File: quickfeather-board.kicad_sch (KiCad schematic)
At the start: 101 parts, among them IC1 EOSAI-S-PUN64, J1 PinHeader_1x2_P2.54mm_Drill1.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, J2 PinHeader_1x12_P2.54m_Drill1.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, J3 61301611121, J4 S2B-PH-SM4-TB(LF)(SN), J5 USB-Micro-B_Molex_473460001, J6 PinHeader_2x5_P1.27mm_SMD_Lat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, J7 PinHeader_1x2_P2.54mm_Drill1.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, J8 PinHeader_2x8_P2.54mm_Drill1mm, Q1 NX3008CBKV, Q2 2N7002PV, Q3 2N7002PV, Q4 DMG1012T-7, U1 TPS62821DLCR, U2 MCP73831T-2AC_SOT, U3 GD25Q16CWIGR, U4 DPS310, U5 MC3635, X1 Resonator_32.768kHz_ECX-31B

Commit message: [#54927] Update components
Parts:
- J2: footprint quickfeather-board-footprints:PinHeader_1x12_P2.54_Drill1.1mm -> quickfeather-board-footprints:PinHeader_1x12_P2.54mm_Drill1.1mm
- J3: footprint quickfeather-board-footprints:PinHeader_1x16_P2.54_Drill1.1mm -> quickfeather-board-footprints:PinHeader_1x16_P2.54mm_Drill1.1mm
- J8: footprint quickfeather-board-footprints:PinHeadder_2x8_P2.54mm_Drill1.1mm -> quickfeather-board-footprints:PinHeader_2x8_P2.54mm_Drill1.1mm
- L1: Val (none) -> 470n/3.6A
- U1: footprint quickfeather-board-footprints:QFN-8_2x1mm -> quickfeather-board-footprints:QFN-8_2x1.5mm
- U4: footprint quickfeather-board-footprints:PG-VLGA-8-2 -> quickfeather-board-footprints:LGA-8_2x2.5mm
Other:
- moved on the sheet: C1, C10, C11, C12, C13, C14, C15, C16, C17, C18, C19, C2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

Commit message: [#54927] Update QFN blend file
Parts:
- IC1: footprint quickfeather-board-footprints:QFN-64-1EP_8.5x8.5mm_P0.5mm_EP3.3x3.3mm -> quickfeather-board-footprints:QFN-64-1EP_8.5x8.5mm_P0.5mm_Layout17x15_EP3.3x3.3mm
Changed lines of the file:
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@@
       (effects (font (size 1.27 1.27)) (justify left bottom) hide)
     )
-    (property "Footprint" "quickfeather-board-footprints:QFN-64-1EP_8.5x8.5mm_P0.5mm_EP3.3x3.3mm" (at 172.72 34.29 0)
+    (property "Footprint" "quickfeather-board-footprints:QFN-64-1EP_8.5x8.5mm_P0.5mm_Layout17x15_EP3.3x3.3mm" (at 172.72 34.29 0)
       (effects (font (size 1.27 1.27)) (justify left bottom) hide)
     )

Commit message: [#54927] Fix DNP
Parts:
- J2, J3, J8, R21, R22, R36: now not fitted; now left out of the parts list
- R42: DNP 1 -> DNP; now not fitted; now left out of the parts list
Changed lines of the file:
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@@
   )
   (symbol (lib_id "quickfeather-board:R_10k_0402") (at 193.675 177.8 270) (unit 1)
-    (in_bom yes) (on_board yes) (dnp no)
+    (in_bom no) (on_board yes) (dnp yes)
     (property "Reference" "R21" (at 194.945 179.07 90)
       (effects (font (size 1.524 1.524)) (justify left))
@@
     )
     (property "DNP" "DNP" (at 193.675 180.34 0)
-      (effects (font (size 1.27 1.27)))
+      (effects (font (size 1.27 1.27)) hide)
     )
     (property "License" "Apache-2.0" (at 168.275 198.12 0)
@@
   )
   (symbol (lib_id "quickfeather-board:R_10k_0402") (at 179.705 182.88 90) (unit 1)
-    (in_bom yes) (on_board yes) (dnp no)
+    (in_bom no) (on_board yes) (dnp yes)
     (property "Reference" "R22" (at 180.975 179.07 90)
       (effects (font (size 1.524 1.524)) (justify right))
@@
     )
     (property "DNP" "DNP" (at 179.705 180.34 0)
-      (effects (font (size 1.27 1.27)))
+      (effects (font (size 1.27 1.27)) hide)
     )
     (property "License" "Apache-2.0" (at 205.105 162.56 0)
@@
   )
   (symbol (lib_id "quickfeather-board:R_10k_0402") (at 255.905 178.435 270) (unit 1)
-    (in_bom yes) (on_board yes) (dnp no)
+    (in_bom no) (on_board yes) (dnp yes)
     (property "Reference" "R36" (at 257.175 179.705 90)
       (effects (font (size 1.524 1.524)) (justify left))
@@
     )
     (property "DNP" "DNP" (at 255.905 179.07 0)
-      (effects (font (size 1.27 1.27)) (justify left))
+      (effects (font (size 1.27 1.27)) (justify left) hide)
     )
     (property "License" "Apache-2.0" (at 230.505 198.755 0)
@@
   )
   (symbol (lib_id "quickfeather-board:PinHeader_2x8_P2.54mm_Drill1.1mm") (at 381 145.415 0) (unit 1)
-    (in_bom yes) (on_board yes) (dnp no)
+    (in_bom no) (on_board yes) (dnp yes)
     (property "Reference" "J8" (at 386.08 140.97 0)
       (effects (font (size 1.27 1.27)))
@@
     )
     (property "DNP" "DNP" (at 386.08 165.735 0)
-      (effects (font (size 1.27 1.27)))
+      (effects (font (size 1.27 1.27)) hide)
     )
     (property "Author" "Antmicro" (at 402.59 161.925 0)
@@
   )
   (symbol (lib_id "quickfeather-board:PinHeader_1x12_P2.54m_Drill1.1mm") (at 360.68 144.145 0) (unit 1)
-    (in_bom yes) (on_board yes) (dnp no)
+    (in_bom no) (on_board yes) (dnp yes)
     (property "Reference" "J2" (at 363.22 141.605 0)
       (effects (font (size 1.27 1.27)) (justify left))
@@
     )
     (property "DNP" "DNP" (at 367.03 172.72 90)
-      (effects (font (size 1.27 1.27)) (justify left))
+      (effects (font (size 1.27 1.27)) (justify left) hide)
     )
     (property "Manufacturer" "Multicomp Pro" (at 381 161.925 0)
@@
   )
   (symbol (lib_id "quickfeather-board:PinHeader_1x16_P2.54mm_Drill1.1mm") (at 360.68 132.08 0) (mirror x) (unit 1)
-    (in_bom yes) (on_board yes) (dnp no)
+    (in_bom no) (on_board yes) (dnp yes)
     (property "Reference" "J3" (at 363.22 92.075 0)
       (effects (font (size 1.27 1.27)) (justify left top))
@@
     )
     (property "DNP" "DNP" (at 366.395 128.905 90)
-      (effects (font (size 1.27 1.27)) (justify left top))
+      (effects (font (size 1.27 1.27)) (justify left top) hide)
     )
     (property "Author" "Antmicro" (at 374.65 114.3 0)
@@
   )
   (symbol (lib_id "quickfeather-board:R_8x22R_0602_array") (at 380.365 189.23 0) (unit 1)
-    (in_bom yes) (on_board yes) (dnp no) (fields_autoplaced)
+    (in_bom no) (on_board yes) (dnp yes) (fields_autoplaced)
     (property "Reference" "R42" (at 385.445 182.88 0)
       (effects (font (size 1.524 1.524)))
@@
       (effects (font (size 1.27 1.27) (thickness 0.15)) (justify left bottom) hide)
     )
-    (property "DNP" "1" (at 380.365 189.23 0)
-      (effects (font (size 1.27 1.27)) hide)
-    )
+    (property "DNP" "DNP" (at 380.365 189.23 0)
+      (effects (font (size 1.27 1.27)) hide)
+    )

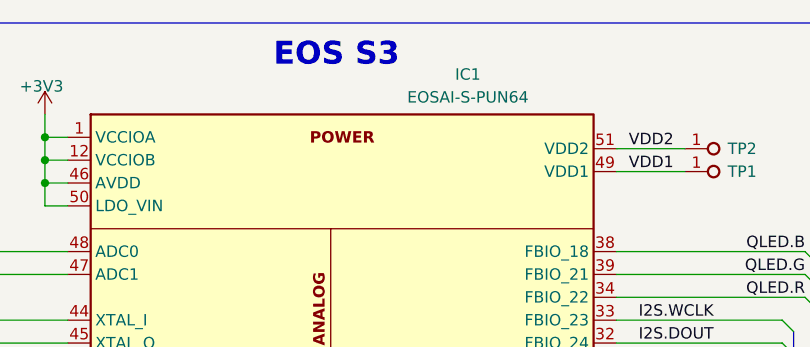
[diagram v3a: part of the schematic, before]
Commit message: [#54927] Change IC1 to U6
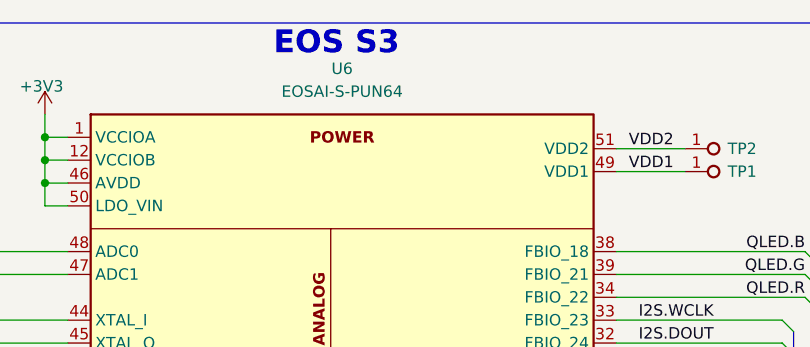
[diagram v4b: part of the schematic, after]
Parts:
- renumbered IC1 to U6
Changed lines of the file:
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@@
     (effects (font (size 2.54 2.54) (thickness 0.508) bold) (justify left bottom))
   )
-  (text "EOS S3" (at 104.14 20.32 0)
+  (text "EOS S3" (at 104.14 19.05 0)
     (effects (font (size 2.54 2.54) (thickness 0.508) bold) (justify left bottom))
   )
@@
   (symbol (lib_id "quickfeather-board:EOSAI-S-PUN64") (at 81.28 27.94 0) (unit 1)
     (in_bom yes) (on_board yes) (dnp no) (fields_autoplaced)
-    (property "Reference" "IC1" (at 125.73 20.955 0)
+    (property "Reference" "U6" (at 111.76 20.32 0)
       (effects (font (size 1.27 1.27)))
     )
@@
       (effects (font (size 1.27 1.27)) (justify left bottom) hide)
     )
-    (property "MPN" "EOSAI-S-PUN64" (at 125.73 23.495 0)
+    (property "MPN" "EOSAI-S-PUN64" (at 111.76 22.86 0)
       (effects (font (size 1.27 1.27)))
     )
@@
       (project "quickfeather-board"
         (path "/902b299f-3bfc-46c5-8ba2-656b16e1e538"
-          (reference "IC1") (unit 1)
+          (reference "U6") (unit 1)
         )
       )

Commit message: [#54927] Change QFN-64 footprint name
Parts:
- U6: footprint quickfeather-board-footprints:QFN-64-1EP_8.5x8.5mm_P0.5mm_Layout17x15_EP3.3x3.3mm -> quickfeather-board-footprints:QFN-64-1EP_8.5x8.5mm_P0.5mm_Lay17x15
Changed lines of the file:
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@@
       (effects (font (size 1.27 1.27)) (justify left bottom) hide)
     )
-    (property "Footprint" "quickfeather-board-footprints:QFN-64-1EP_8.5x8.5mm_P0.5mm_Layout17x15_EP3.3x3.3mm" (at 172.72 34.29 0)
+    (property "Footprint" "quickfeather-board-footprints:QFN-64-1EP_8.5x8.5mm_P0.5mm_Lay17x15" (at 172.72 34.29 0)
       (effects (font (size 1.27 1.27)) (justify left bottom) hide)
     )
